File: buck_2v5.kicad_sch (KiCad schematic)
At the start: 20 parts, among them U3 TPS564257DRLR

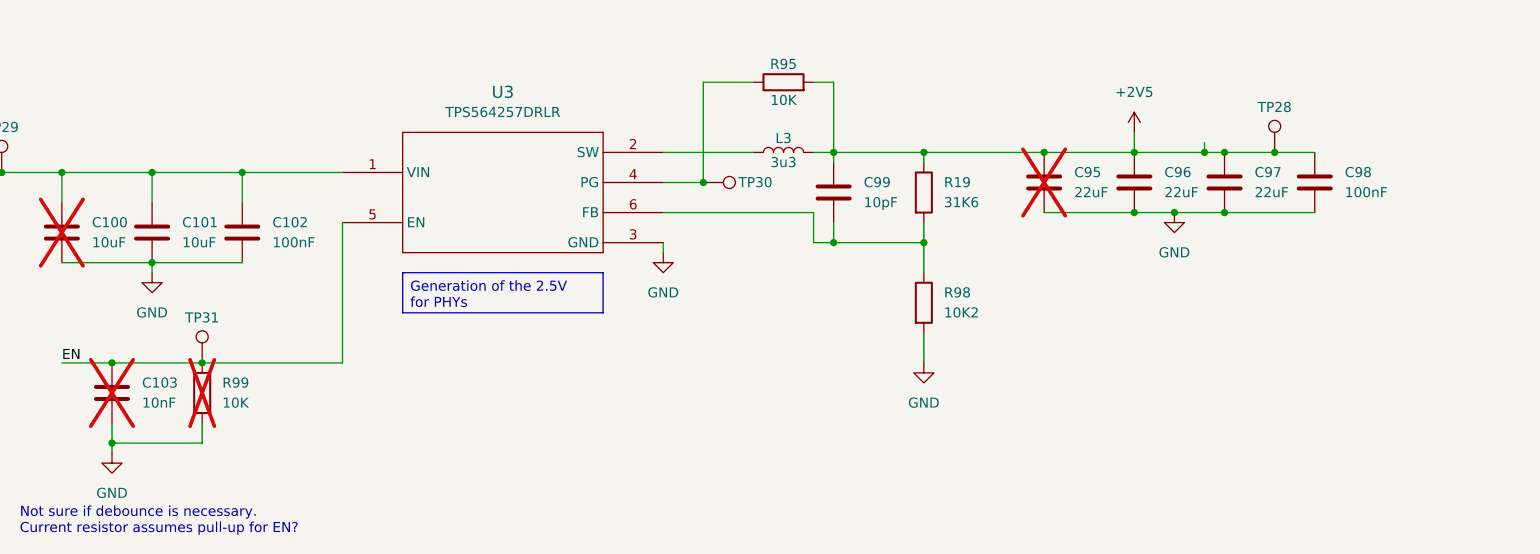
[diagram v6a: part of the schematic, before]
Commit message: fixing issue related to symbol changes, and updating components
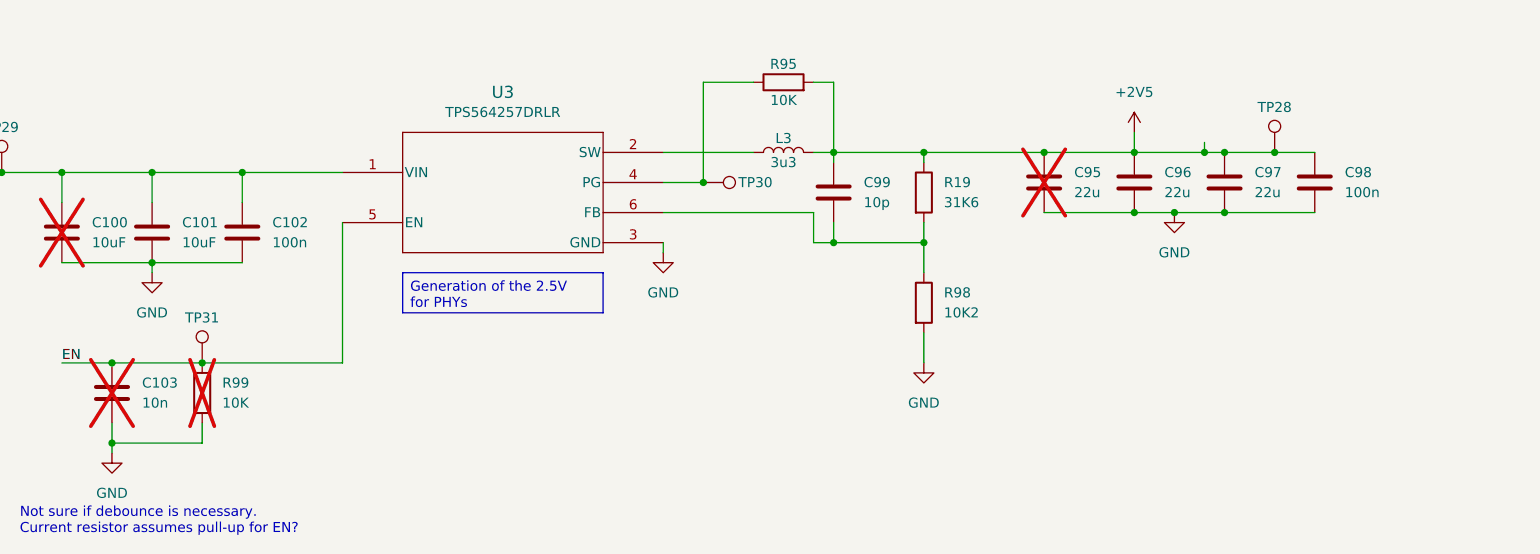
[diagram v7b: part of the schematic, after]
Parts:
- C100, C101: footprint KL:C_0603 -> Capacitor_SMD:C_0201_0603Metric; symbol KL_C:C_10uF_25V_X5R_0603_20 -> KL_C:C_10u_25V_X5R_0603_20
- C102: value 100nF -> 100n; footprint KL:C_0603 -> Capacitor_SMD:C_0201_0603Metric; symbol KL_C:C_100nF_16V_X7R_0603_10 -> KL_C:C_100n_16V_X7R_0603_10
- C103: value 10nF -> 10n; footprint KL:C_0603 -> Capacitor_SMD:C_0201_0603Metric; symbol KL_C:C_10nF_25V_X7R_0603_20 -> KL_C:C_10n_50V_X7R_0603_10; Digikey 311-3111-1-ND -> 1276-CL10B103KB8WPNDCT-ND; LCSC C726559 -> C307346; Mouser 603-AC603KRX7R8BB103 -> 187-CL10B103KB8WPND; Tolerance 20 -> 10; Voltage 25 -> 50; now in the parts list
- C95, C96, C97: value 22uF -> 22u; symbol KL_C:C_22uF_10V_X5R_0603_20 -> KL_C:C_22u_10V_X5R_0603_20; Digikey 490-10476-1-ND -> 490-13243-1-ND; LCSC C84419 -> C361061; Mouser 81-GRM188R61A226ME5D -> 81-GRM187R61A226ME5D
- C98: value 100nF -> 100n; footprint KL:C_0603 -> Capacitor_SMD:C_0201_0603Metric; symbol KL_C:C_100nF_10V_X7R_0603_10 -> KL_C:C_100n_10V_X7R_0603_10
- C99: value 10pF -> 10p; symbol KL_C:C_10pF_25V_C0G_0603_5 -> KL_C:C_10p_25V_C0G_0603_5
- R98, R99: footprint KL:R_0603 -> KL_Footprints:C_0603
- U3: footprint KL:SOT-563 -> KL_Footprints:SOT-563; symbol KL_IC_Power:TI_TPS564357DRLR -> KL_Voltage_Regulators:TPS564257DRLR; LCSC (none) -> C19272233; Mouser 595-TPS564257DRLR -> 595-TPS564257DRLR
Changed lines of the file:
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@@
 	)
 	(symbol
-		(lib_id "KL_C:C_100nF_16V_X7R_0603_10")
+		(lib_id "KL_C:C_100n_16V_X7R_0603_10")
 		(at 99.06 88.9 0)
 		(unit 1)
@@
 			)
 		)
-		(property "Value" "100nF"
+		(property "Value" "100n"
 			(at 102.87 90.1699 0)
 			(effects
@@
 			)
 		)
-		(property "Footprint" "KL:C_0603"
+		(property "Footprint" "Capacitor_SMD:C_0201_0603Metric"
 			(at 100.0252 92.71 0)
 			(effects
@@
 	)
 	(symbol
-		(lib_id "KL_C:C_100nF_10V_X7R_0603_10")
+		(lib_id "KL_C:C_100n_10V_X7R_0603_10")
 		(at 234.95 82.55 0)
 		(unit 1)
@@
 			)
 		)
-		(property "Value" "100nF"
+		(property "Value" "100n"
 			(at 238.76 83.8199 0)
 			(effects
@@
 			)
 		)
-		(property "Footprint" "KL:C_0603"
+		(property "Footprint" "Capacitor_SMD:C_0201_0603Metric"
 			(at 235.9152 86.36 0)
 			(effects
@@
 			)
 		)
-		(property "Footprint" "KL:R_0603"
+		(property "Footprint" "KL_Footprints:C_0603"
 			(at 183.642 97.79 90)
 			(effects
@@
 	)
 	(symbol
-		(lib_id "KL_C:C_22uF_10V_X5R_0603_20")
+		(lib_id "KL_C:C_22u_10V_X5R_0603_20")
 		(at 212.09 82.55 0)
 		(unit 1)
@@
 			)
 		)
-		(property "Value" "22uF"
+		(property "Value" "22u"
 			(at 215.9 83.8199 0)
 			(effects
@@
 			)
 		)
-		(property "Mouser" "81-GRM188R61A226ME5D"
+		(property "Mouser" "81-GRM187R61A226ME5D"
 			(at 212.09 82.55 0)
 			(effects
@@
 			)
 		)
-		(property "Digikey" "490-10476-1-ND"
+		(property "Digikey" "490-13243-1-ND"
 			(at 212.09 82.55 0)
 			(effects
@@
 			)
 		)
-		(property "LCSC" "C84419"
+		(property "LCSC" "C361061"
 			(at 212.09 82.55 0)
 			(effects
@@
 		(dnp no)
 		(fields_autoplaced yes)
-		(property "Reference" "#PWR020"
+		(property "Reference" "#PWR20"
 			(at 185.42 111.76 0)
 			(effects
@@
 			(project "shish-lan"
 				(path "/d4536448-b109-4159-96e2-3dc21baf2d6e/0b7d9af9-83c1-43fa-a7a0-a33d0a00ea9c/c6e71b93-7134-487d-a04c-584c6081214b"
-					(reference "#PWR020")
+					(reference "#PWR20")
 					(unit 1)
 				)
@@
 	)
 	(symbol
-		(lib_id "KL_C:C_10uF_25V_X5R_0603_20")
+		(lib_id "KL_C:C_10u_25V_X5R_0603_20")
 		(at 76.2 88.9 0)
 		(unit 1)
@@
 			)
 		)
-		(property "Footprint" "KL:C_0603"
+		(property "Footprint" "Capacitor_SMD:C_0201_0603Metric"
 			(at 77.1652 92.71 0)
 			(effects
@@
 		(dnp no)
 		(fields_autoplaced yes)
-		(property "Reference" "#PWR017"
+		(property "Reference" "#PWR17"
 			(at 217.17 92.71 0)
 			(effects
@@
 			(project "shish-lan"
 				(path "/d4536448-b109-4159-96e2-3dc21baf2d6e/0b7d9af9-83c1-43fa-a7a0-a33d0a00ea9c/c6e71b93-7134-487d-a04c-584c6081214b"
-					(reference "#PWR017")
+					(reference "#PWR17")
 					(unit 1)
 				)
@@
 	)
 	(symbol
-		(lib_name "R_10K_100mW_5_0603_1")
 		(lib_id "KL_R:R_10K_100mW_5_0603")
 		(at 167.64 69.85 90)
@@
 	)
 	(symbol
-		(lib_id "KL_IC_Power:TI_TPS564357DRLR")
-		(at 132.08 83.82 0)
+		(lib_id "KL_Voltage_Regulators:TPS564257DRLR")
+		(at 111.76 81.28 0)
 		(unit 1)
 		(exclude_from_sim no)
@@
 			)
 		)
-		(property "Footprint" "KL:SOT-563"
-			(at 132.08 78.74 0)
-			(effects
-				(font
-					(size 1.27 1.27)
-				)
-				(hide yes)
-			)
-		)
-		(property "Datasheet" ""
-			(at 132.08 78.74 0)
-			(effects
-				(font
-					(size 1.27 1.27)
+		(property "Footprint" "KL_Footprints:SOT-563"
+			(at 111.76 81.28 0)
+			(effects
+				(font
+					(size 1.27 1.27)
+					(italic yes)
+				)
+				(hide yes)
+			)
+		)
+		(property "Datasheet" "https://www.ti.com/lit/gpn/tps564257"
+			(at 111.76 81.28 0)
+			(effects
+				(font
+					(size 1.27 1.27)
+					(italic yes)
 				)
 				(hide yes)
@@
 		)
 		(property "Description" ""
-			(at 132.08 78.74 0)
-			(effects
-				(font
-					(size 1.27 1.27)
-				)
-				(hide yes)
-			)
-		)
-		(property "Mouser" "595-TPS564257DRLR"
-			(at 132.08 83.82 0)
+			(at 111.76 81.28 0)
+			(effects
+				(font
+					(size 1.27 1.27)
+				)
+				(hide yes)
+			)
+		)
+		(property "Mouser" " 595-TPS564257DRLR "
+			(at 111.76 81.28 0)
 			(effects
 				(font
@@
 		)
 		(property "Digikey" "296-TPS564257DRLRCT-ND"
-			(at 132.08 83.82 0)
+			(at 111.76 81.28 0)
 			(effects
 				(font
@@
 		)
 		(property "LSCS" "C19272233"
-			(at 132.08 83.82 0)
+			(at 111.76 81.28 0)
+			(effects
+				(font
+					(size 1.27 1.27)
+				)
+				(hide yes)
+			)
+		)
+		(property "LCSC" "C19272233"
+			(at 111.76 81.28 0)
 			(effects
 				(font
@@
 		(dnp no)
 		(fields_autoplaced yes)
-		(property "Reference" "#PWR021"
+		(property "Reference" "#PWR21"
 			(at 82.55 123.19 0)
 			(effects
@@
 			(project "shish-lan"
 				(path "/d4536448-b109-4159-96e2-3dc21baf2d6e/0b7d9af9-83c1-43fa-a7a0-a33d0a00ea9c/c6e71b93-7134-487d-a04c-584c6081214b"
-					(reference "#PWR021")
+					(reference "#PWR21")
 					(unit 1)
 				)
@@
 	)
 	(symbol
-		(lib_id "KL_C:C_10nF_25V_X7R_0603_20")
+		(lib_id "KL_C:C_10n_50V_X7R_0603_10")
 		(at 82.55 109.22 0)
 		(unit 1)
 		(exclude_from_sim no)
-		(in_bom no)
+		(in_bom yes)
 		(on_board yes)
 		(dnp yes)
@@
 			)
 		)
-		(property "Value" "10nF"
+		(property "Value" "10n"
 			(at 86.36 110.4899 0)
 			(effects
@@
 			)
 		)
-		(property "Footprint" "KL:C_0603"
+		(property "Footprint" "Capacitor_SMD:C_0201_0603Metric"
 			(at 83.5152 113.03 0)
 			(effects
@@
 			)
 		)
-		(property "Tolerance" "20"
+		(property "Tolerance" "10"
 			(at 82.55 109.22 0)
 			(effects
@@
 			)
 		)
-		(property "Voltage" "25"
+		(property "Voltage" "50"
 			(at 82.55 109.22 0)
 			(effects
@@
 			)
 		)
-		(property "Mouser" "603-AC603KRX7R8BB103"
+		(property "Mouser" "187-CL10B103KB8WPND"
 			(at 82.55 109.22 0)
 			(effects
@@
 			)
 		)
-		(property "Digikey" "311-3111-1-ND"
+		(property "Digikey" "1276-CL10B103KB8WPNDCT-ND"
 			(at 82.55 109.22 0)
 			(effects
@@
 			)
 		)
-		(property "LCSC" "C726559"
+		(property "LCSC" "C307346"
 			(at 82.55 109.22 0)
 			(effects
@@
 		(dnp no)
 		(fields_autoplaced yes)
-		(property "Reference" "#PWR018"
+		(property "Reference" "#PWR18"
 			(at 152.4 97.79 0)
 			(effects
@@
 			(project "shish-lan"
 				(path "/d4536448-b109-4159-96e2-3dc21baf2d6e/0b7d9af9-83c1-43fa-a7a0-a33d0a00ea9c/c6e71b93-7134-487d-a04c-584c6081214b"
-					(reference "#PWR018")
+					(reference "#PWR18")
 					(unit 1)
 				)
@@
 		(dnp no)
 		(fields_autoplaced yes)
-		(property "Reference" "#PWR019"
+		(property "Reference" "#PWR19"
 			(at 87.63 100.33 0)
 			(effects
@@
 			(project "shish-lan"
 				(path "/d4536448-b109-4159-96e2-3dc21baf2d6e/0b7d9af9-83c1-43fa-a7a0-a33d0a00ea9c/c6e71b93-7134-487d-a04c-584c6081214b"
-					(reference "#PWR019")
+					(reference "#PWR19")
 					(unit 1)
 				)
@@
 	)
 	(symbol
-		(lib_id "KL_C:C_22uF_10V_X5R_0603_20")
+		(lib_id "KL_C:C_22u_10V_X5R_0603_20")
 		(at 223.52 82.55 0)
 		(unit 1)
@@
 			)
 		)
-		(property "Value" "22uF"
+		(property "Value" "22u"
 			(at 227.33 83.8199 0)
 			(effects
@@
 			)
 		)
-		(property "Mouser" "81-GRM188R61A226ME5D"
+		(property "Mouser" "81-GRM187R61A226ME5D"
 			(at 223.52 82.55 0)
 			(effects
@@
 			)
 		)
-		(property "Digikey" "490-10476-1-ND"
+		(property "Digikey" "490-13243-1-ND"
 			(at 223.52 82.55 0)
 			(effects
@@
 			)
 		)
-		(property "LCSC" "C84419"
+		(property "LCSC" "C361061"
 			(at 223.52 82.55 0)
 			(effects
@@
 			)
 		)
-		(property "Footprint" "KL:R_0603"
+		(property "Footprint" "KL_Footprints:C_0603"
 			(at 92.202 109.22 90)
 			(effects
@@
 	)
 	(symbol
-		(lib_id "KL_C:C_22uF_10V_X5R_0603_20")
+		(lib_id "KL_C:C_22u_10V_X5R_0603_20")
 		(at 200.66 82.55 0)
 		(unit 1)
@@
 			)
 		)
-		(property "Value" "22uF"
+		(property "Value" "22u"
 			(at 204.47 83.8199 0)
 			(effects
@@
 			)
 		)
-		(property "Mouser" "81-GRM188R61A226ME5D"
+		(property "Mouser" "81-GRM187R61A226ME5D"
 			(at 200.66 82.55 0)
 			(effects
@@
 			)
 		)
-		(property "Digikey" "490-10476-1-ND"
+		(property "Digikey" "490-13243-1-ND"
 			(at 200.66 82.55 0)
 			(effects
@@
 			)
 		)
-		(property "LCSC" "C84419"
+		(property "LCSC" "C361061"
 			(at 200.66 82.55 0)
 			(effects
@@
 	)
 	(symbol
-		(lib_id "KL_C:C_10pF_25V_C0G_0603_5")
+		(lib_id "KL_C:C_10p_25V_C0G_0603_5")
 		(at 173.99 83.82 0)
 		(unit 1)
@@
 			)
 		)
-		(property "Value" "10pF"
+		(property "Value" "10p"
 			(at 177.8 85.0899 0)
 			(effects
@@
 	)
 	(symbol
-		(lib_id "KL_C:C_10uF_25V_X5R_0603_20")
+		(lib_id "KL_C:C_10u_25V_X5R_0603_20")
 		(at 87.63 88.9 0)
 		(unit 1)
@@
 			)
 		)
-		(property "Footprint" "KL:C_0603"
+		(property "Footprint" "Capacitor_SMD:C_0201_0603Metric"
 			(at 88.5952 92.71 0)
 			(effects
@@
 		(dnp no)
 		(fields_autoplaced yes)
-		(property "Reference" "#PWR03"
+		(property "Reference" "#PWR3"
 			(at 212.09 80.01 0)
 			(effects
@@
 			(project "shish-lan"
 				(path "/d4536448-b109-4159-96e2-3dc21baf2d6e/0b7d9af9-83c1-43fa-a7a0-a33d0a00ea9c/c6e71b93-7134-487d-a04c-584c6081214b"
-					(reference "#PWR03")
-					(unit 1)
-				)
+					(reference "#PWR3")
+					(unit 1)
+				)

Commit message: updates all symbols to the project only paths. My bad - sorry
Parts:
- C100, C95, R99: now in the parts list
- U3: LSCS C19272233 -> (none)
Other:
- moved on the sheet: TP30
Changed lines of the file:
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@@
+	)
+	(junction
+		(at 158.75 69.85)
+		(diameter 0)
+		(color 0 0 0 0)
 	)
 	(junction
@@
 	)
 	(junction
-		(at 157.48 82.55)
-		(diameter 0)
-		(color 0 0 0 0)
-	)
-	(junction
 		(at 87.63 92.71)
 		(diameter 0)
@@
 	(wire
 		(pts
-			(xy 163.83 69.85) (xy 157.48 69.85)
+			(xy 163.83 69.85) (xy 158.75 69.85)
 		)
 		(stroke
@@
 		(pts
 			(xy 223.52 78.74) (xy 220.98 78.74)
+		)
+		(stroke
+			(width 0)
+			(type default)
+		)
+	)
+	(wire
+		(pts
+			(xy 158.75 69.85) (xy 157.48 69.85)
 		)
 		(stroke
@@
 		(on_board yes)
 		(dnp no)
+		(fields_autoplaced yes)
 		(property "Reference" "R96"
-			(at 62.23 78.74 90)
+			(at 62.23 74.93 90)
 			(effects
 				(font
@@
 		)
 		(property "Value" "0R"
-			(at 62.23 83.82 90)
+			(at 62.23 77.47 90)
 			(effects
 				(font
@@
 		(unit 1)
 		(exclude_from_sim no)
-		(in_bom no)
+		(in_bom yes)
 		(on_board yes)
 		(dnp yes)
@@
 		(on_board yes)
 		(dnp no)
+		(fields_autoplaced yes)
 		(property "Reference" "R95"
-			(at 167.64 67.564 90)
+			(at 167.64 63.5 90)
 			(effects
 				(font
@@
 		)
 		(property "Value" "10K"
-			(at 167.64 72.136 90)
+			(at 167.64 66.04 90)
 			(effects
 				(font
@@
 			(effects
 				(font
-					(size 1.27 1.27)
+					(size 1.524 1.524)
 				)
 			)
@@
 		)
 		(property "Digikey" "296-TPS564257DRLRCT-ND"
-			(at 111.76 81.28 0)
-			(effects
-				(font
-					(size 1.27 1.27)
-				)
-				(hide yes)
-			)
-		)
-		(property "LSCS" "C19272233"
 			(at 111.76 81.28 0)
 			(effects
@@
 	(symbol
 		(lib_id "KL_TP:TestPoint")
-		(at 157.48 82.55 270)
+		(at 158.75 69.85 0)
 		(unit 1)
 		(exclude_from_sim no)
@@
 		(fields_autoplaced yes)
 		(property "Reference" "TP30"
-			(at 164.084 82.55 90)
+			(at 158.75 64.135 0)
 			(do_not_autoplace yes)
 			(effects
@@
 		)
 		(property "Value" "~"
-			(at 162.56 82.55 0)
+			(at 158.75 64.77 0)
 			(effects
 				(font
@@
 		)
 		(property "Footprint" "Connector_PinHeader_2.54mm:PinHeader_1x01_P2.54mm_Vertical"
-			(at 157.48 87.63 0)
+			(at 163.83 69.85 0)
 			(effects
 				(font
@@
 		)
 		(property "Datasheet" "~"
-			(at 157.48 87.63 0)
+			(at 163.83 69.85 0)
 			(effects
 				(font
@@
 		)
 		(property "Description" "test point"
-			(at 157.48 82.55 0)
+			(at 158.75 69.85 0)
 			(effects
 				(font
@@
 		(unit 1)
 		(exclude_from_sim no)
-		(in_bom no)
+		(in_bom yes)
 		(on_board yes)
 		(dnp yes)
@@
 		(unit 1)
 		(exclude_from_sim no)
-		(in_bom no)
+		(in_bom yes)
 		(on_board yes)
 		(dnp yes)
